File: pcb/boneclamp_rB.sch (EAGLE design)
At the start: 73 parts, among them IC1 24C, U1 AD8032ARZ-REEL7, U2 LT1964ES5-5TRMPBF, U4 TLV70245DBVT, U7 AD7682BCPZ, U8 TPS63700DRCT, U9 ADA4841-2YRZ

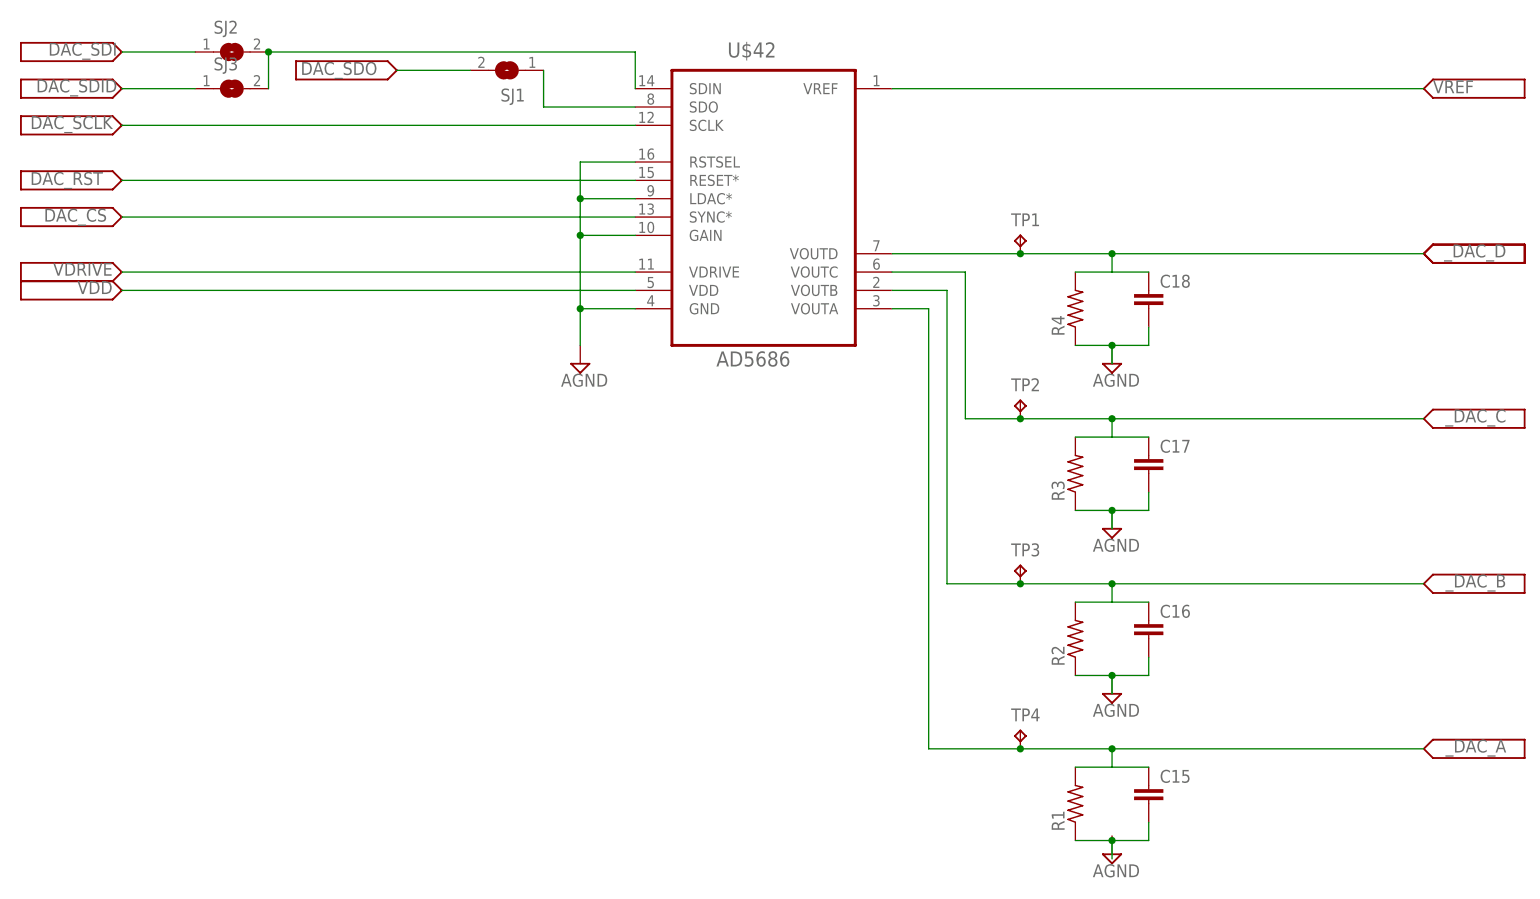
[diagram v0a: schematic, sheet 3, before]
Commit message: Properly bypassed the power and logic supplies for the DAC
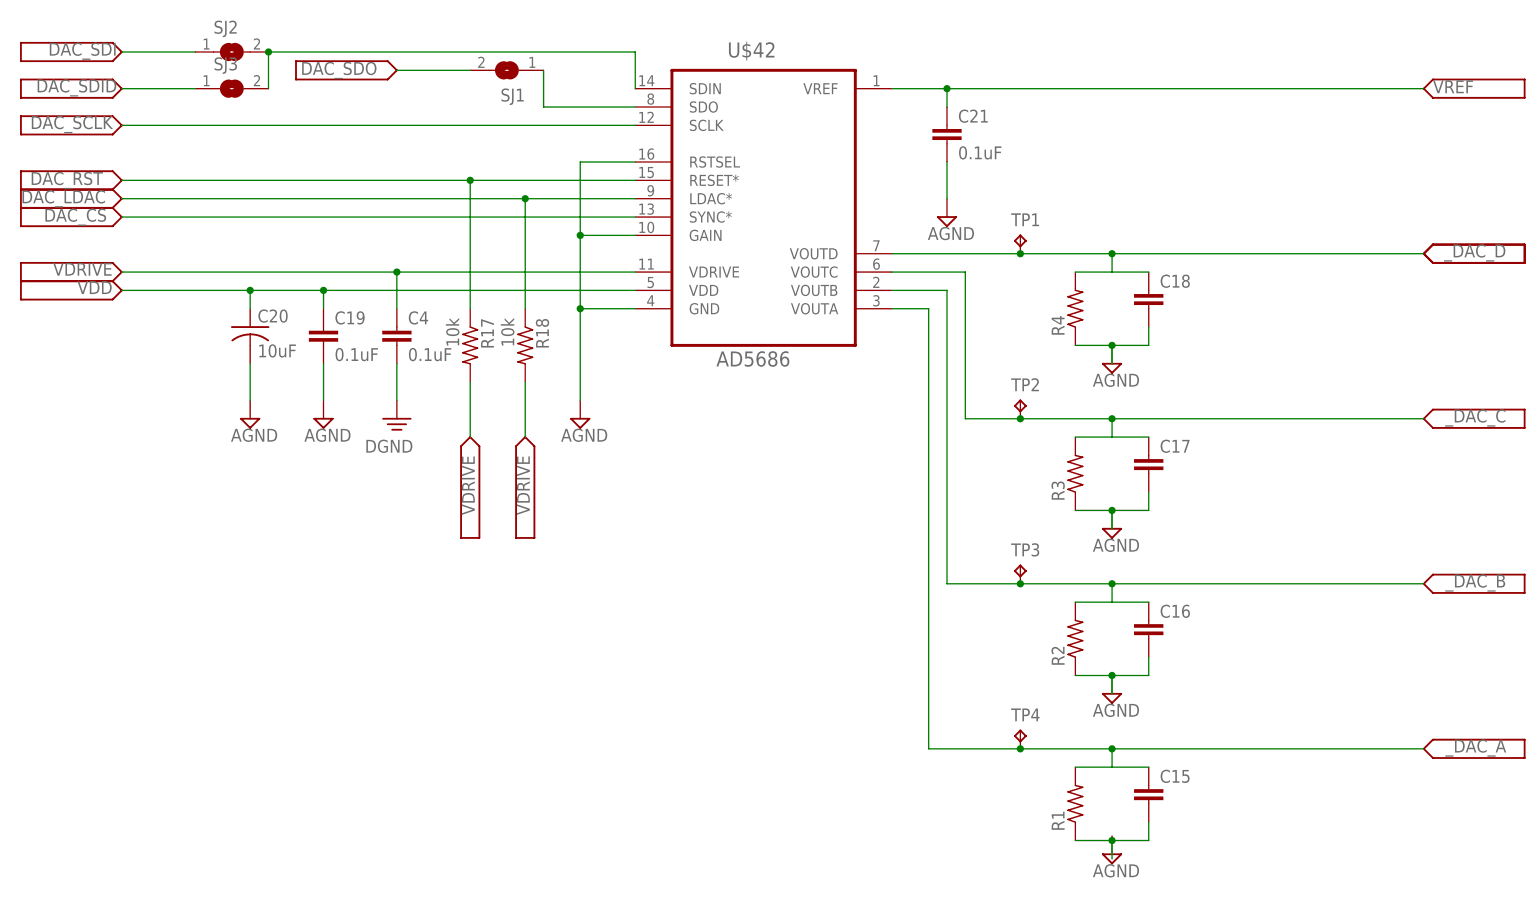
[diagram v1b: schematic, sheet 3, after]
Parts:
- added C19, C21, C4: 0.1uF, rcl:C-EUC0805
- added C20: 10uF, rcl:C-USC0805
- added R17, R18: 10k, rcl:R-US_R0805
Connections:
- new net DAC_LDAC: R18.1, U$42.LDAC*
- new net PE: C4.2
- net AGND: now also C19.2, C20.2, C21.2; no longer U$42.LDAC*
- net DAC_RST: now also R17.1
- net VDD: now also C19.1, C20.1
- net VDRIVE: now also C4.1, R17.2, R18.2
- net VREF: now also C21.1
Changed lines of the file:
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@@
 <part name="TP7" library="testpad" deviceset="TP" device="B1,27"/>
 <part name="C3" library="rcl" deviceset="C-EU" device="C0805" value="10uF"/>
+<part name="DGND1" library="supply2" deviceset="PE" device="" value="DGND"/>
+<part name="C4" library="rcl" deviceset="C-EU" device="C0805" value="0.1uF"/>
+<part name="C19" library="rcl" deviceset="C-EU" device="C0805" value="0.1uF"/>
+<part name="C20" library="rcl" deviceset="C-US" device="C0805" value="10uF"/>
+<part name="SUPPLY5" library="supply2" deviceset="AGND" device=""/>
+<part name="SUPPLY6" library="supply2" deviceset="AGND" device=""/>
+<part name="C21" library="rcl" deviceset="C-EU" device="C0805" value="0.1uF"/>
+<part name="SUPPLY7" library="supply2" deviceset="AGND" device=""/>
+<part name="R17" library="rcl" deviceset="R-US_" device="R0805" value="10k"/>
+<part name="R18" library="rcl" deviceset="R-US_" device="R0805" value="10k"/>
+<part name="U$27" library="boneclamp" deviceset="V_SIG" device=""/>
+<part name="U$28" library="boneclamp" deviceset="V_SIG" device=""/>
+<part name="U$60" library="boneclamp" deviceset="V_SIG" device=""/>
 </parts>
 <sheets>
@@
 <instance part="U$55" gate="G$1" x="91.44" y="-7.62"/>
 <instance part="U$56" gate="G$1" x="91.44" y="15.24"/>
-<instance part="SUPPLY2" gate="G$1" x="-25.4" y="-22.86"/>
+<instance part="SUPPLY2" gate="G$1" x="-25.4" y="-30.48"/>
 <instance part="U$57" gate="G$1" x="-88.9" y="10.16" rot="R180"/>
 <instance part="U$58" gate="G$1" x="-88.9" y="-2.54" rot="R180"/>
 <instance part="U$59" gate="G$1" x="-88.9" y="2.54" rot="R180"/>
+<instance part="DGND1" gate="PE" x="-50.8" y="-30.48"/>
+<instance part="C4" gate="G$1" x="-50.8" y="-17.78"/>
+<instance part="C19" gate="G$1" x="-60.96" y="-17.78"/>
+<instance part="C20" gate="G$1" x="-71.12" y="-17.78"/>
+<instance part="SUPPLY5" gate="G$1" x="-60.96" y="-30.48"/>
+<instance part="SUPPLY6" gate="G$1" x="-71.12" y="-30.48"/>
+<instance part="C21" gate="G$1" x="25.4" y="10.16"/>
+<instance part="SUPPLY7" gate="G$1" x="25.4" y="-2.54"/>
+<instance part="R17" gate="G$1" x="-40.64" y="-20.32" rot="R270"/>
+<instance part="R18" gate="G$1" x="-33.02" y="-20.32" rot="R270"/>
+<instance part="U$27" gate="G$1" x="-40.64" y="-33.02" rot="R270"/>
+<instance part="U$28" gate="G$1" x="-88.9" y="0" rot="R180"/>
+<instance part="U$60" gate="G$1" x="-33.02" y="-33.02" rot="R270"/>
 </instances>
 <busses>
@@
 <net name="VDD" class="0">
 <segment>
-<wire x1="-17.78" y1="-12.7" x2="-88.9" y2="-12.7" width="0.1524" layer="91"/>
+<wire x1="-17.78" y1="-12.7" x2="-60.96" y2="-12.7" width="0.1524" layer="91"/>
 <label x="-90.17" y="-11.43" size="1.778" layer="95" rot="R180"/>
 <pinref part="U$42" gate="G$1" pin="VDD"/>
+<pinref part="C20" gate="G$1" pin="1"/>
+<wire x1="-60.96" y1="-12.7" x2="-71.12" y2="-12.7" width="0.1524" layer="91"/>
+<wire x1="-71.12" y1="-12.7" x2="-88.9" y2="-12.7" width="0.1524" layer="91"/>
+<wire x1="-71.12" y1="-15.24" x2="-71.12" y2="-12.7" width="0.1524" layer="91"/>
+<junction x="-71.12" y="-12.7"/>
+<pinref part="C19" gate="G$1" pin="1"/>
+<wire x1="-60.96" y1="-15.24" x2="-60.96" y2="-12.7" width="0.1524" layer="91"/>
+<junction x="-60.96" y="-12.7"/>
 </segment>
 </net>
@@
 <segment>
 <pinref part="SUPPLY2" gate="G$1" pin="AGND"/>
-<wire x1="-25.4" y1="-20.32" x2="-25.4" y2="-15.24" width="0.1524" layer="91"/>
+<wire x1="-25.4" y1="-27.94" x2="-25.4" y2="-15.24" width="0.1524" layer="91"/>
 <pinref part="U$42" gate="G$1" pin="GND"/>
 <wire x1="-25.4" y1="-15.24" x2="-17.78" y2="-15.24" width="0.1524" layer="91"/>
@@
 <wire x1="-25.4" y1="-5.08" x2="-25.4" y2="-15.24" width="0.1524" layer="91"/>
 <junction x="-25.4" y="-15.24"/>
-<pinref part="U$42" gate="G$1" pin="LDAC*"/>
-<wire x1="-17.78" y1="0" x2="-25.4" y2="0" width="0.1524" layer="91"/>
-<wire x1="-25.4" y1="0" x2="-25.4" y2="-5.08" width="0.1524" layer="91"/>
 <junction x="-25.4" y="-5.08"/>
 <pinref part="U$42" gate="G$1" pin="RSTSEL"/>
 <wire x1="-17.78" y1="5.08" x2="-25.4" y2="5.08" width="0.1524" layer="91"/>
-<wire x1="-25.4" y1="5.08" x2="-25.4" y2="0" width="0.1524" layer="91"/>
-<junction x="-25.4" y="0"/>
+<wire x1="-25.4" y1="5.08" x2="-25.4" y2="-5.08" width="0.1524" layer="91"/>
+</segment>
+<segment>
+<pinref part="SUPPLY6" gate="G$1" pin="AGND"/>
+<pinref part="C20" gate="G$1" pin="2"/>
+<wire x1="-71.12" y1="-27.94" x2="-71.12" y2="-22.86" width="0.1524" layer="91"/>
+</segment>
+<segment>
+<pinref part="SUPPLY5" gate="G$1" pin="AGND"/>
+<pinref part="C19" gate="G$1" pin="2"/>
+<wire x1="-60.96" y1="-27.94" x2="-60.96" y2="-22.86" width="0.1524" layer="91"/>
+</segment>
+<segment>
+<pinref part="C21" gate="G$1" pin="2"/>
+<pinref part="SUPPLY7" gate="G$1" pin="AGND"/>
+<wire x1="25.4" y1="5.08" x2="25.4" y2="0" width="0.1524" layer="91"/>
 </segment>
 </net>
 <net name="VDRIVE" class="0">
 <segment>
-<wire x1="-17.78" y1="-10.16" x2="-88.9" y2="-10.16" width="0.1524" layer="91"/>
+<wire x1="-17.78" y1="-10.16" x2="-50.8" y2="-10.16" width="0.1524" layer="91"/>
 <label x="-90.17" y="-8.89" size="1.778" layer="95" rot="R180"/>
 <pinref part="U$42" gate="G$1" pin="VDRIVE"/>
+<pinref part="C4" gate="G$1" pin="1"/>
+<wire x1="-50.8" y1="-10.16" x2="-88.9" y2="-10.16" width="0.1524" layer="91"/>
+<wire x1="-50.8" y1="-15.24" x2="-50.8" y2="-10.16" width="0.1524" layer="91"/>
+<junction x="-50.8" y="-10.16"/>
+</segment>
+<segment>
+<pinref part="R17" gate="G$1" pin="2"/>
+<wire x1="-40.64" y1="-25.4" x2="-40.64" y2="-33.02" width="0.1524" layer="91"/>
+<label x="-40.005" y="-43.815" size="1.778" layer="95" rot="R90"/>
+</segment>
+<segment>
+<pinref part="R18" gate="G$1" pin="2"/>
+<wire x1="-33.02" y1="-25.4" x2="-33.02" y2="-33.02" width="0.1524" layer="91"/>
+<label x="-32.385" y="-43.815" size="1.778" layer="95" rot="R90"/>
 </segment>
 </net>
@@
 <segment>
 <pinref part="U$42" gate="G$1" pin="VREF"/>
-<wire x1="17.78" y1="15.24" x2="91.44" y2="15.24" width="0.1524" layer="91"/>
+<wire x1="17.78" y1="15.24" x2="25.4" y2="15.24" width="0.1524" layer="91"/>
 <label x="92.71" y="14.605" size="1.778" layer="95"/>
+<pinref part="C21" gate="G$1" pin="1"/>
+<wire x1="25.4" y1="15.24" x2="91.44" y2="15.24" width="0.1524" layer="91"/>
+<wire x1="25.4" y1="12.7" x2="25.4" y2="15.24" width="0.1524" layer="91"/>
+<junction x="25.4" y="15.24"/>
 </segment>
 </net>
@@
 <segment>
 <pinref part="U$42" gate="G$1" pin="RESET*"/>
-<wire x1="-17.78" y1="2.54" x2="-88.9" y2="2.54" width="0.1524" layer="91"/>
+<wire x1="-17.78" y1="2.54" x2="-40.64" y2="2.54" width="0.1524" layer="91"/>
 <label x="-101.6" y="1.905" size="1.778" layer="95"/>
+<pinref part="R17" gate="G$1" pin="1"/>
+<wire x1="-40.64" y1="2.54" x2="-88.9" y2="2.54" width="0.1524" layer="91"/>
+<wire x1="-40.64" y1="-15.24" x2="-40.64" y2="2.54" width="0.1524" layer="91"/>
+<junction x="-40.64" y="2.54"/>
 </segment>
 </net>
@@
 </segment>
 </net>
+<net name="PE" class="0">
+<segment>
+<pinref part="C4" gate="G$1" pin="2"/>
+<pinref part="DGND1" gate="PE" pin="PE"/>
+<wire x1="-50.8" y1="-22.86" x2="-50.8" y2="-27.94" width="0.1524" layer="91"/>
+</segment>
+</net>
+<net name="DAC_LDAC" class="0">
+<segment>
+<pinref part="R18" gate="G$1" pin="1"/>
+<wire x1="-33.02" y1="-15.24" x2="-33.02" y2="0" width="0.1524" layer="91"/>
+<pinref part="U$42" gate="G$1" pin="LDAC*"/>
+<wire x1="-88.9" y1="0" x2="-33.02" y2="0" width="0.1524" layer="91"/>
+<junction x="-33.02" y="0"/>
+<wire x1="-33.02" y1="0" x2="-17.78" y2="0" width="0.1524" layer="91"/>
+<label x="-102.87" y="-0.635" size="1.778" layer="95"/>
+</segment>
+</net>

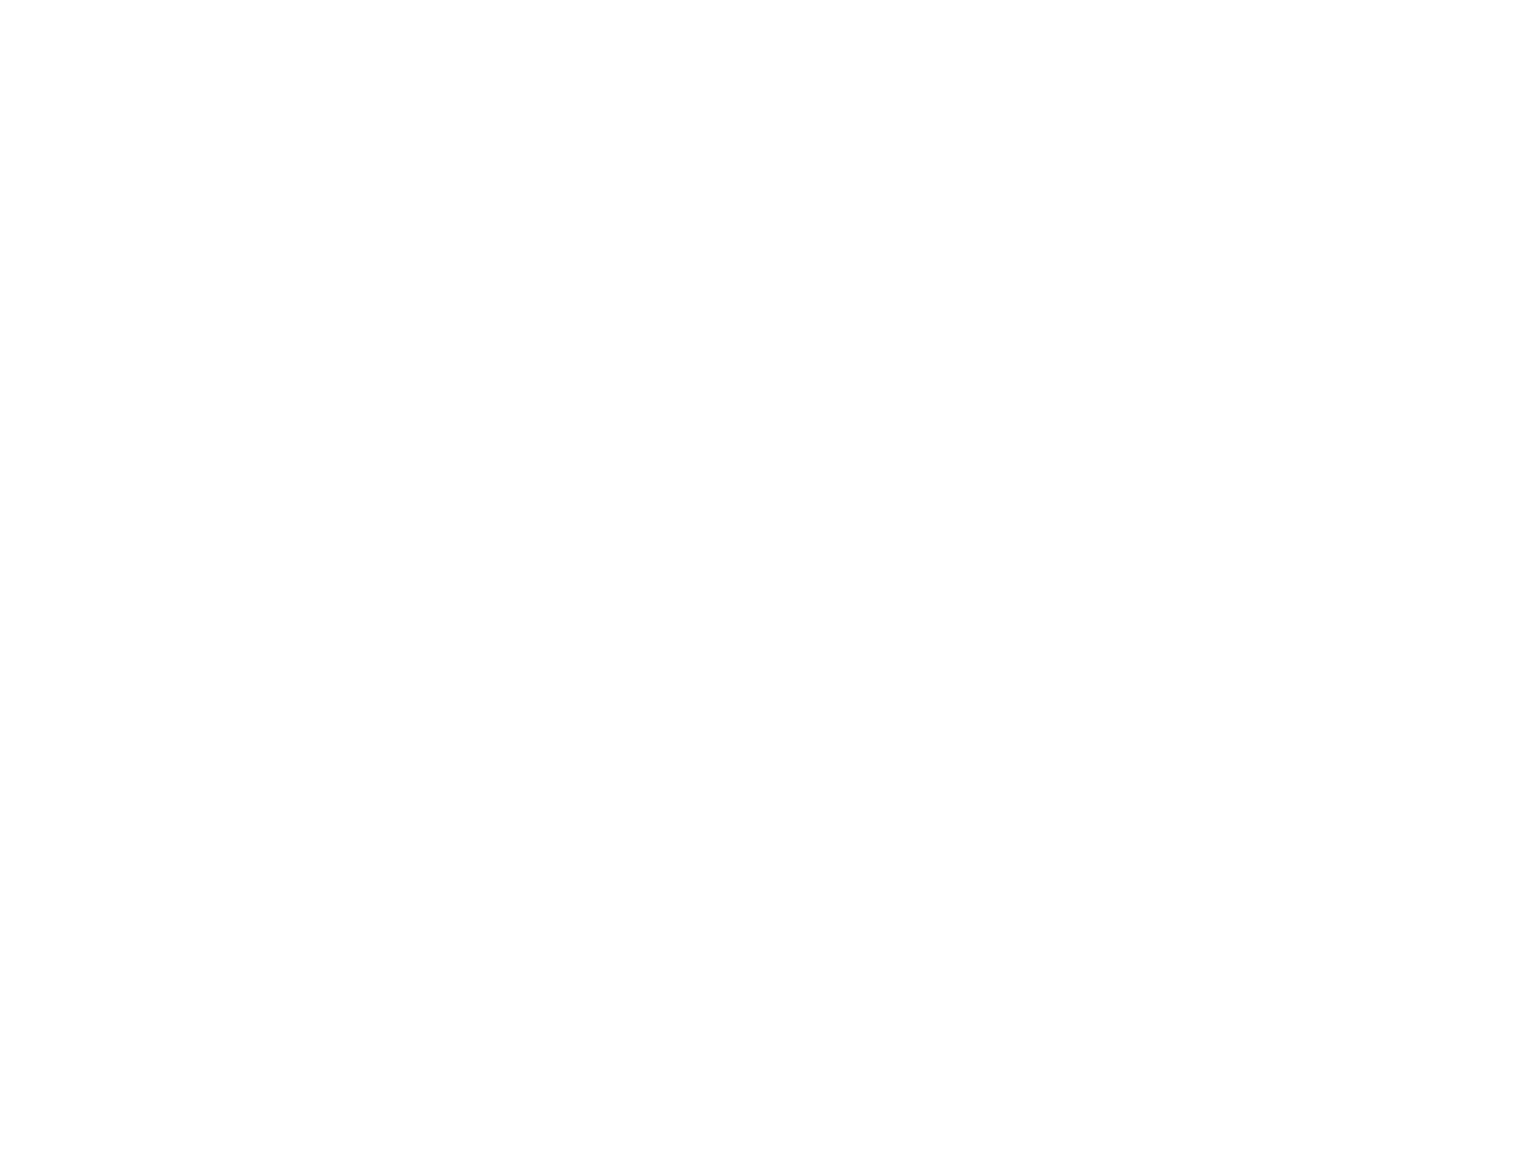
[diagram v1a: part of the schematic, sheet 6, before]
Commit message: Added Stefano's biasing circuitry back into the master branch schematic. Automatic merge was not going to work properly
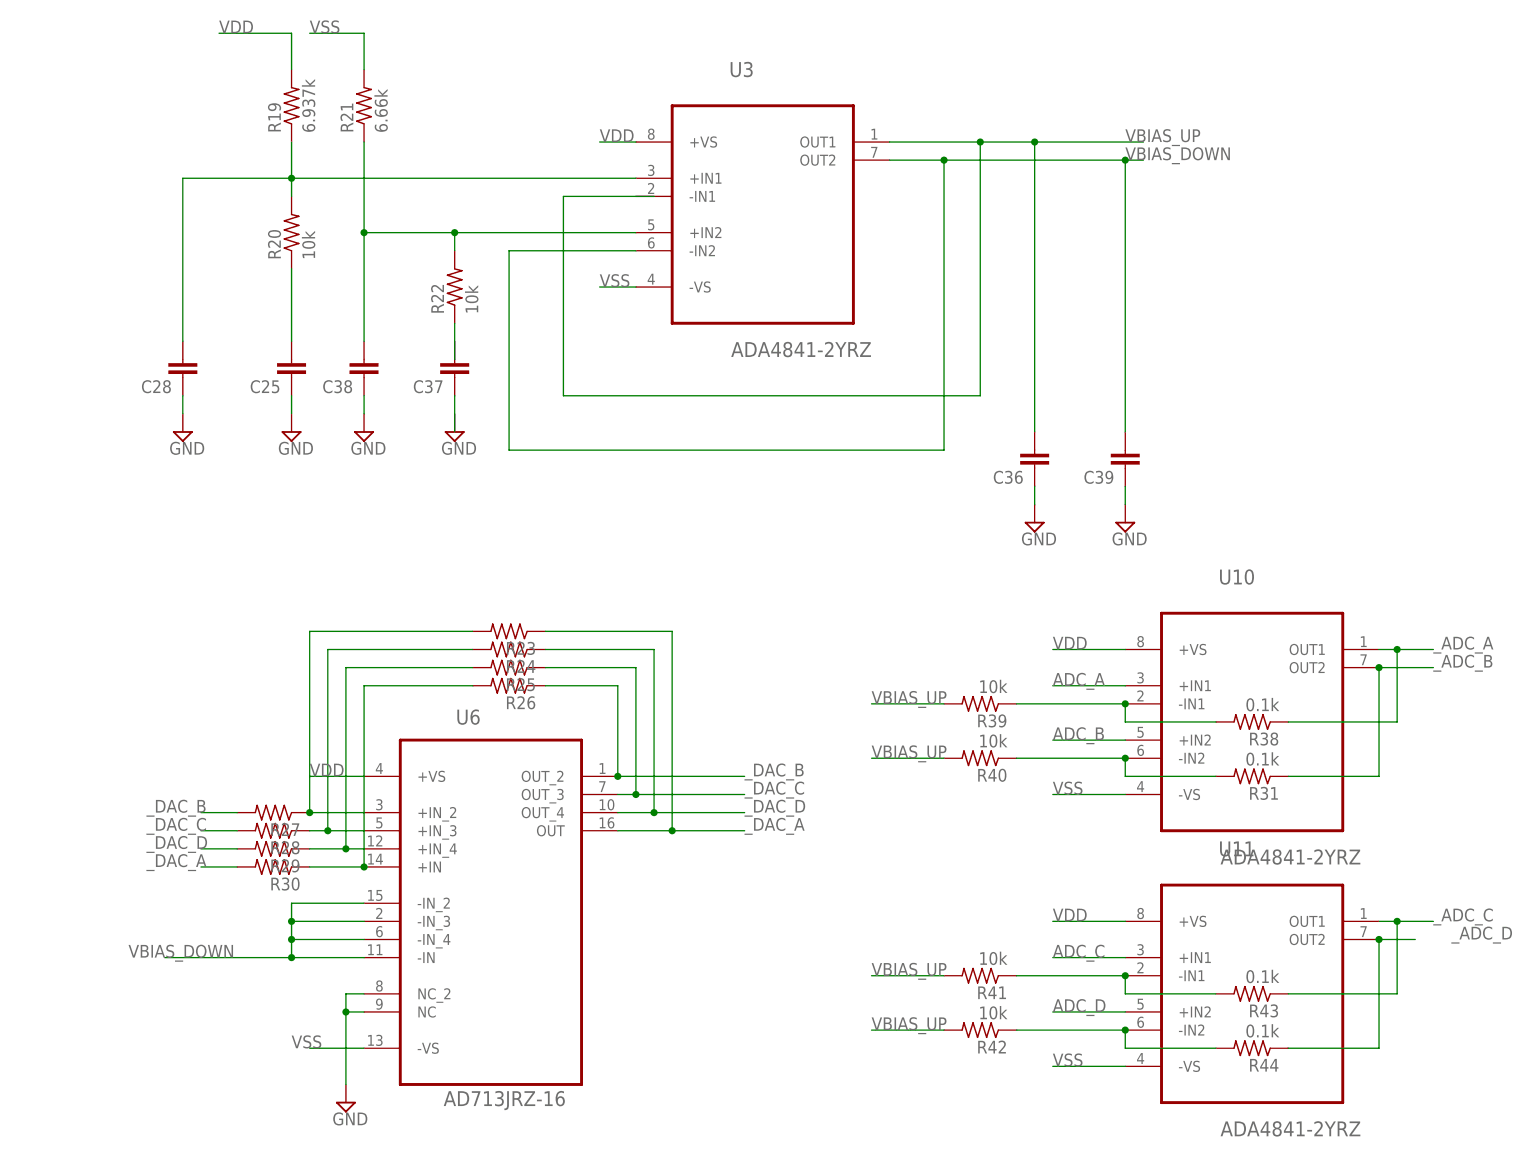
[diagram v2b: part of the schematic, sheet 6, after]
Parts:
- added C25, C28, C36, C37, C38, C39: (no value), resistor:C-EU025-025X050
- added R19: 6.937k, resistor:R-US_0204/2V
- added R20, R22: 10k, resistor:R-US_0204/2V
- added R21: 6.66k, resistor:R-US_0204/2V
- added R23, R24, R25, R26, R27, R28, R29, R30: (no value), resistor:R-US_0204/2V
- added R31, R38, R43, R44: 0.1k, rcl:R-US_R0805
- added R39, R40, R41, R42: 10k, rcl:R-US_R0805
- added U10, U11, U3: ADA4841-2YRZ, analog-devices-01:ADA4841-2YRZ
- added U6: AD713JRZ-16, analog-devices-01:AD713JRZ-16
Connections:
- new net GND: C25.1, C28.1, C36.1, C38.1, C39.1, U6.NC, U6.NC_2
- new net N$3: R26.2, R30.1, U6.+IN
- new net N$52: R25.2, R29.1, U6.+IN_4
- new net N$53: C38.2, R21.1, R22.2, U3.+IN2
- new net N$54: C28.2, R19.1, R20.2, U3.+IN1
- new net N$55: R24.2, R28.1, U6.+IN_3
- new net N$56: R23.2, R27.1, U6.+IN_2
- new net N$57: C25.2, R20.1
- new net N$58: C37.1
- new net N$59: R22.1
- new net VBIAS_DOWN: C39.2, U3.-IN2, U3.OUT2, U6.-IN, U6.-IN_2, U6.-IN_3, U6.-IN_4
- new net VBIAS_UP: C36.2, R31.2, R38.2, R39.1, R39.2, R40.1, R40.2, R41.1, R41.2, R42.1, R42.2, R43.2, R44.2, U10.-IN1, U10.-IN2, U11.-IN1, U11.-IN2, U3.-IN1, U3.OUT1
- net ADC_A: now also U10.+IN1
- net ADC_B: now also U10.+IN2
- net ADC_C: now also U11.+IN1
- net ADC_D: now also U11.+IN2
- net VDD: now also R19.2, U10.+VS, U11.+VS, U3.+VS, U6.+VS
- net VSS: now also R21.2, U10.-VS, U11.-VS, U3.-VS, U6.-VS
- net _ADC_A: now also R38.1, U10.OUT1
- net _ADC_B: now also R31.1, U10.OUT2
- net _ADC_C: now also R43.1, U11.OUT1
- net _ADC_D: now also R44.1, U11.OUT2
- net _DAC_A: now also R23.1, R30.2, U6.OUT
- net _DAC_B: now also R26.1, R27.2, U6.OUT_2
- net _DAC_C: now also R25.1, R28.2, U6.OUT_3
- net _DAC_D: now also R24.1, R29.2, U6.OUT_4
